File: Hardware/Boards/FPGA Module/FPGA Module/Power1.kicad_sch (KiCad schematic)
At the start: 84 parts, among them U10 TPS62933O, U12 INA700AYWFR, U13 INA700AYWFR, U14 INA700AYWFR, U15 INA700AYWFR, U16 INA700AYWFR, U18 INA236, U19 TPS74801AWDRC, U2 TPS62933O, U3 AOZ2369QI-11, U4 TPSM33625RDNR, U7 TPS62933O, U8 TPS62933O, U9 TPS62933O

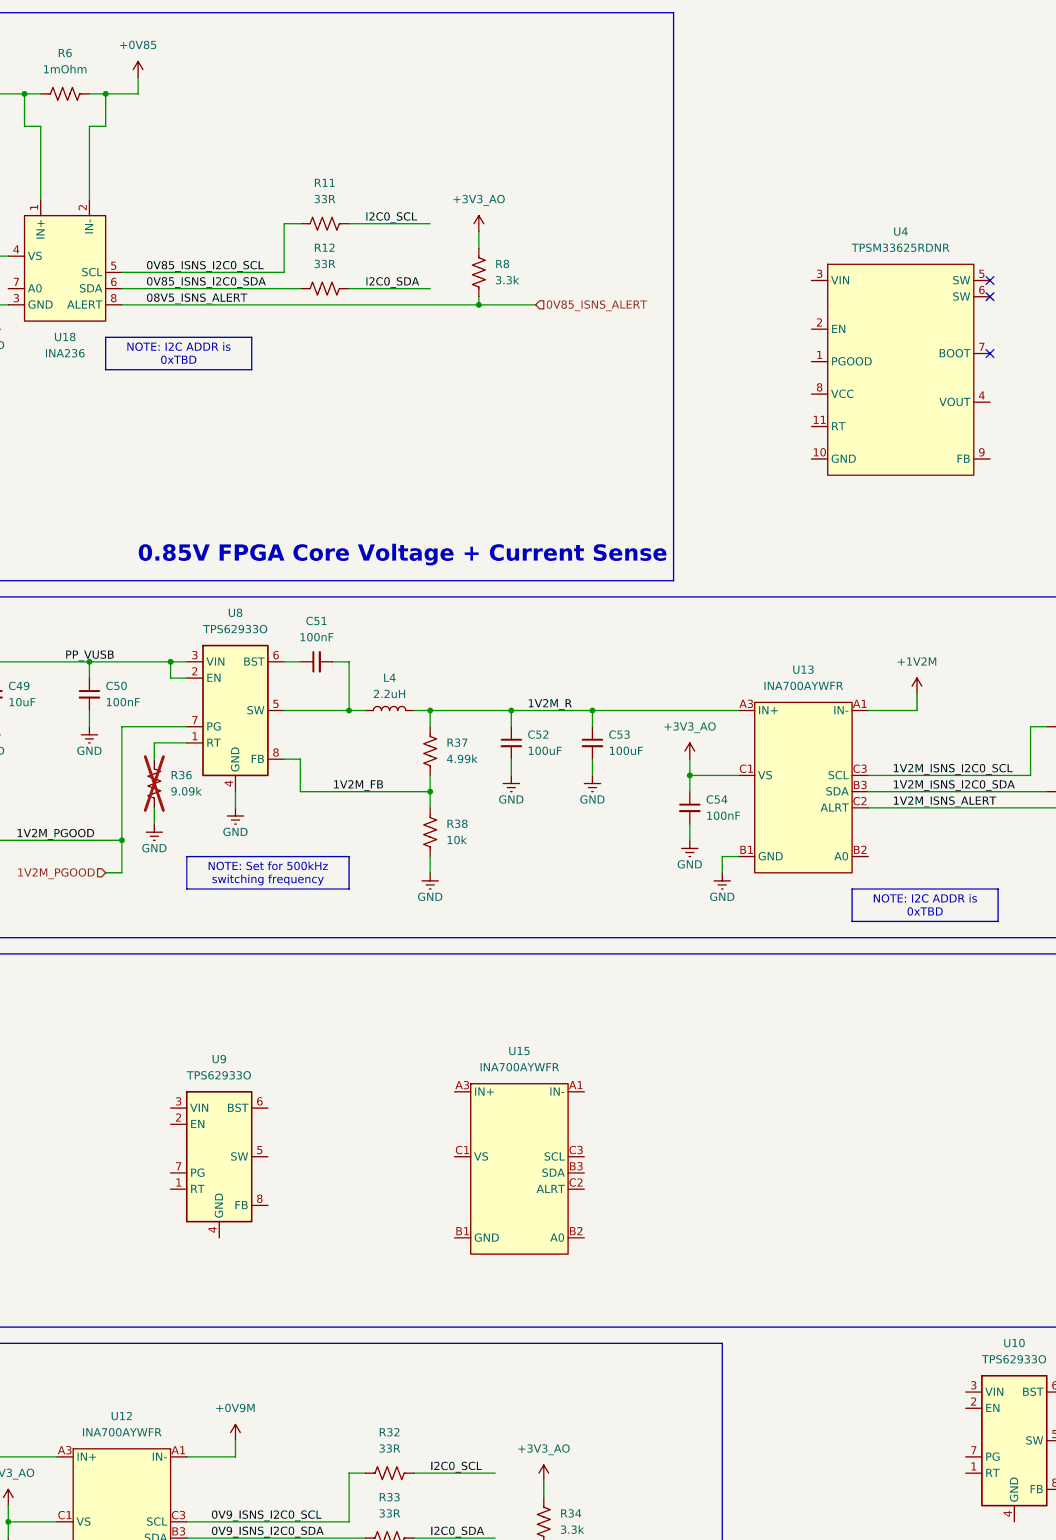
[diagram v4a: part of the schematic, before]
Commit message: Using new DP to HDMI IC
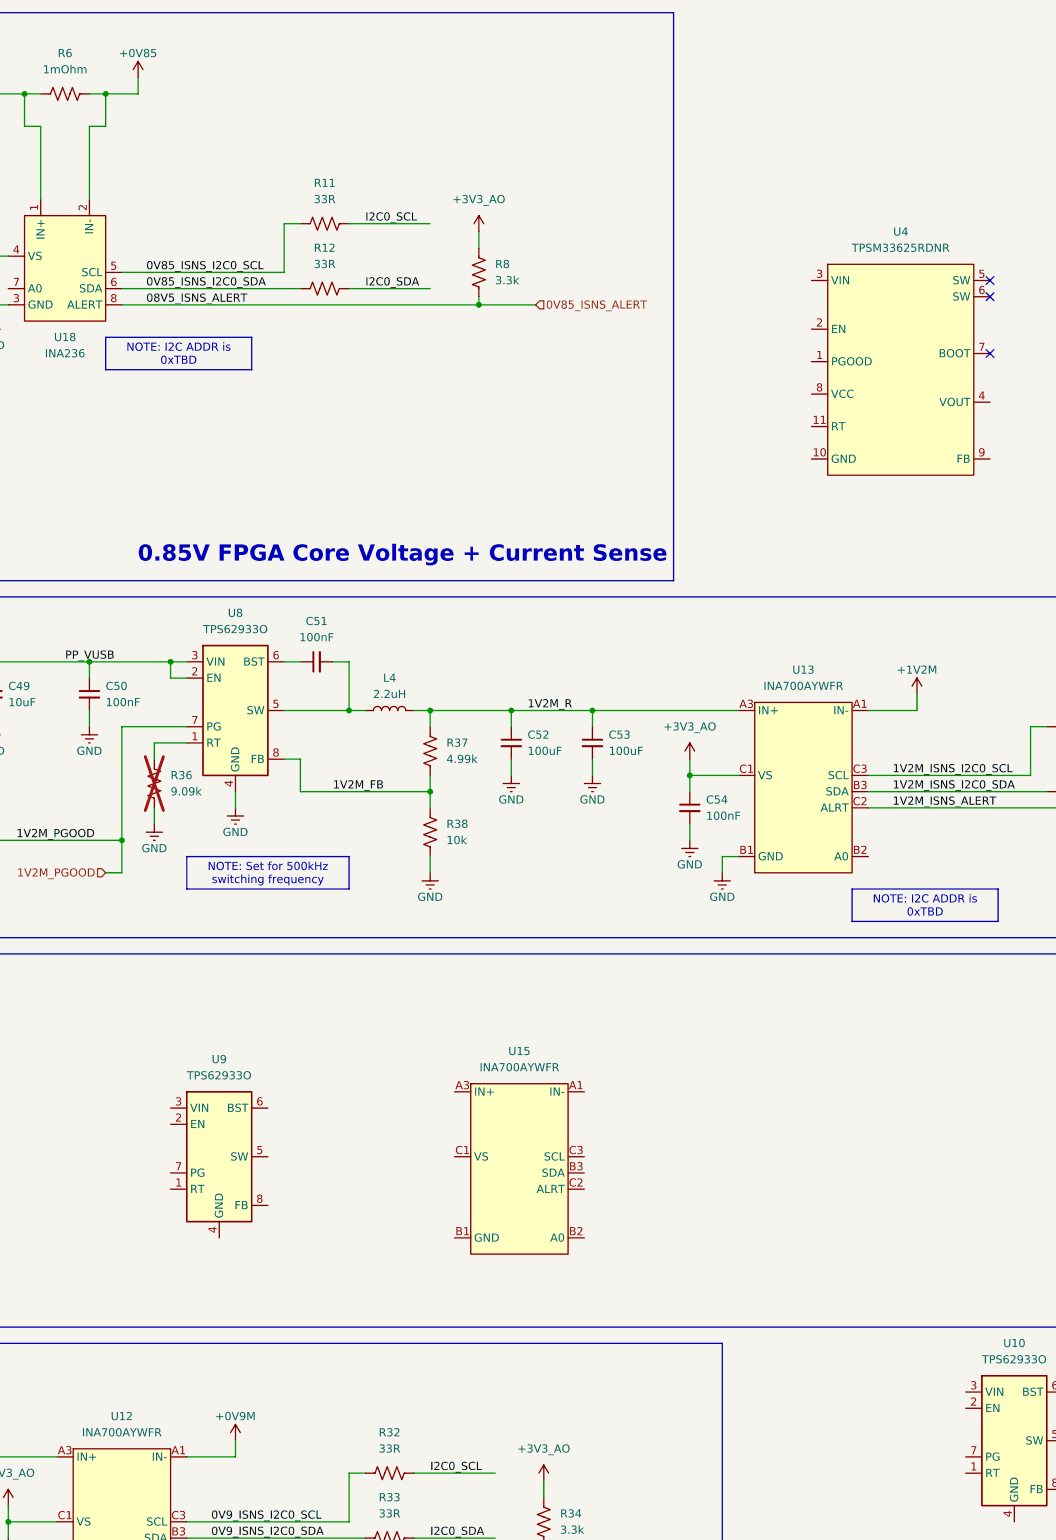
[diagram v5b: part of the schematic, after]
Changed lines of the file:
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@@
 		(on_board yes)
 		(dnp no)
-		(fields_autoplaced yes)
 		(property "Reference" "#PWR0100"
 			(at 297.18 125.73 0)
@@
 		)
 		(property "Value" "+1V2M"
-			(at 297.18 116.84 0)
+			(at 297.18 118.11 0)
 			(effects
 				(font
@@
 		(on_board yes)
 		(dnp no)
-		(fields_autoplaced yes)
 		(property "Reference" "#PWR085"
 			(at 190.5 242.57 0)
@@
 		)
 		(property "Value" "+0V9M"
-			(at 190.5 233.68 0)
+			(at 190.5 234.95 0)
 			(effects
 				(font
@@
 		(on_board yes)
 		(dnp no)
-		(fields_autoplaced yes)
 		(property "Reference" "#PWR027"
 			(at 175.26 29.21 0)
@@
 		)
 		(property "Value" "+0V85"
-			(at 175.26 20.32 0)
+			(at 175.26 21.59 0)
 			(effects
 				(font

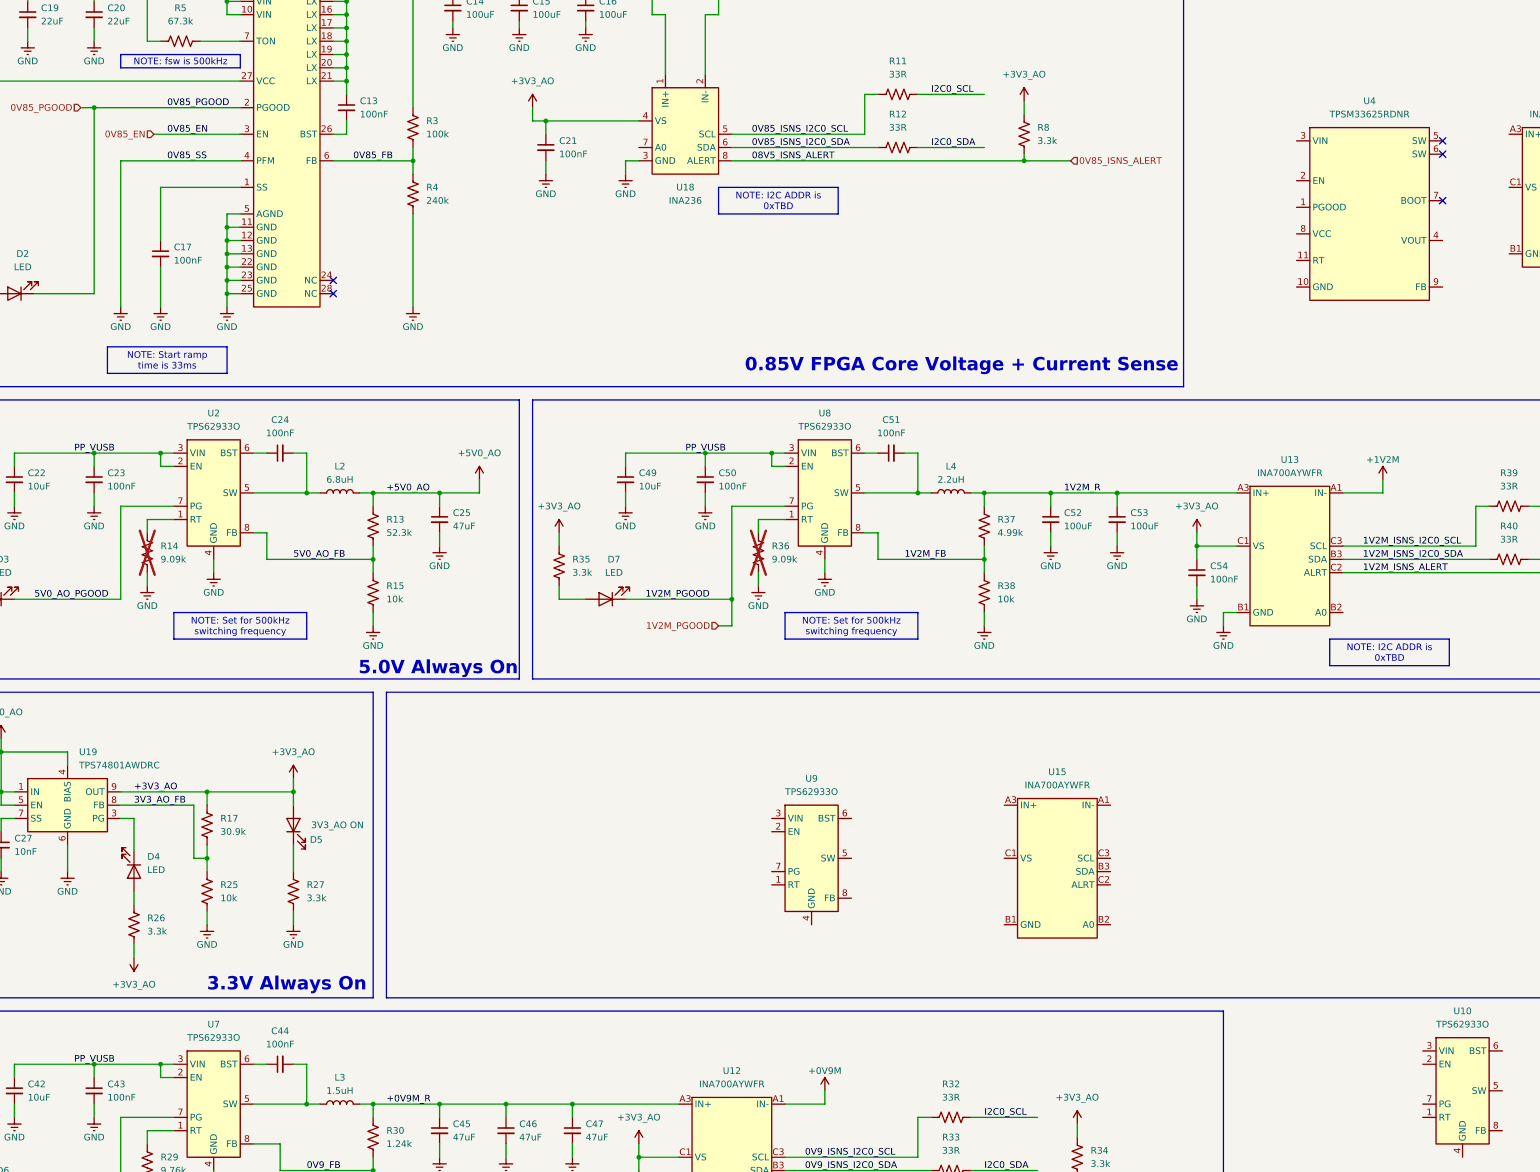
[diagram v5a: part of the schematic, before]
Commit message: minor FPGA schematic changes
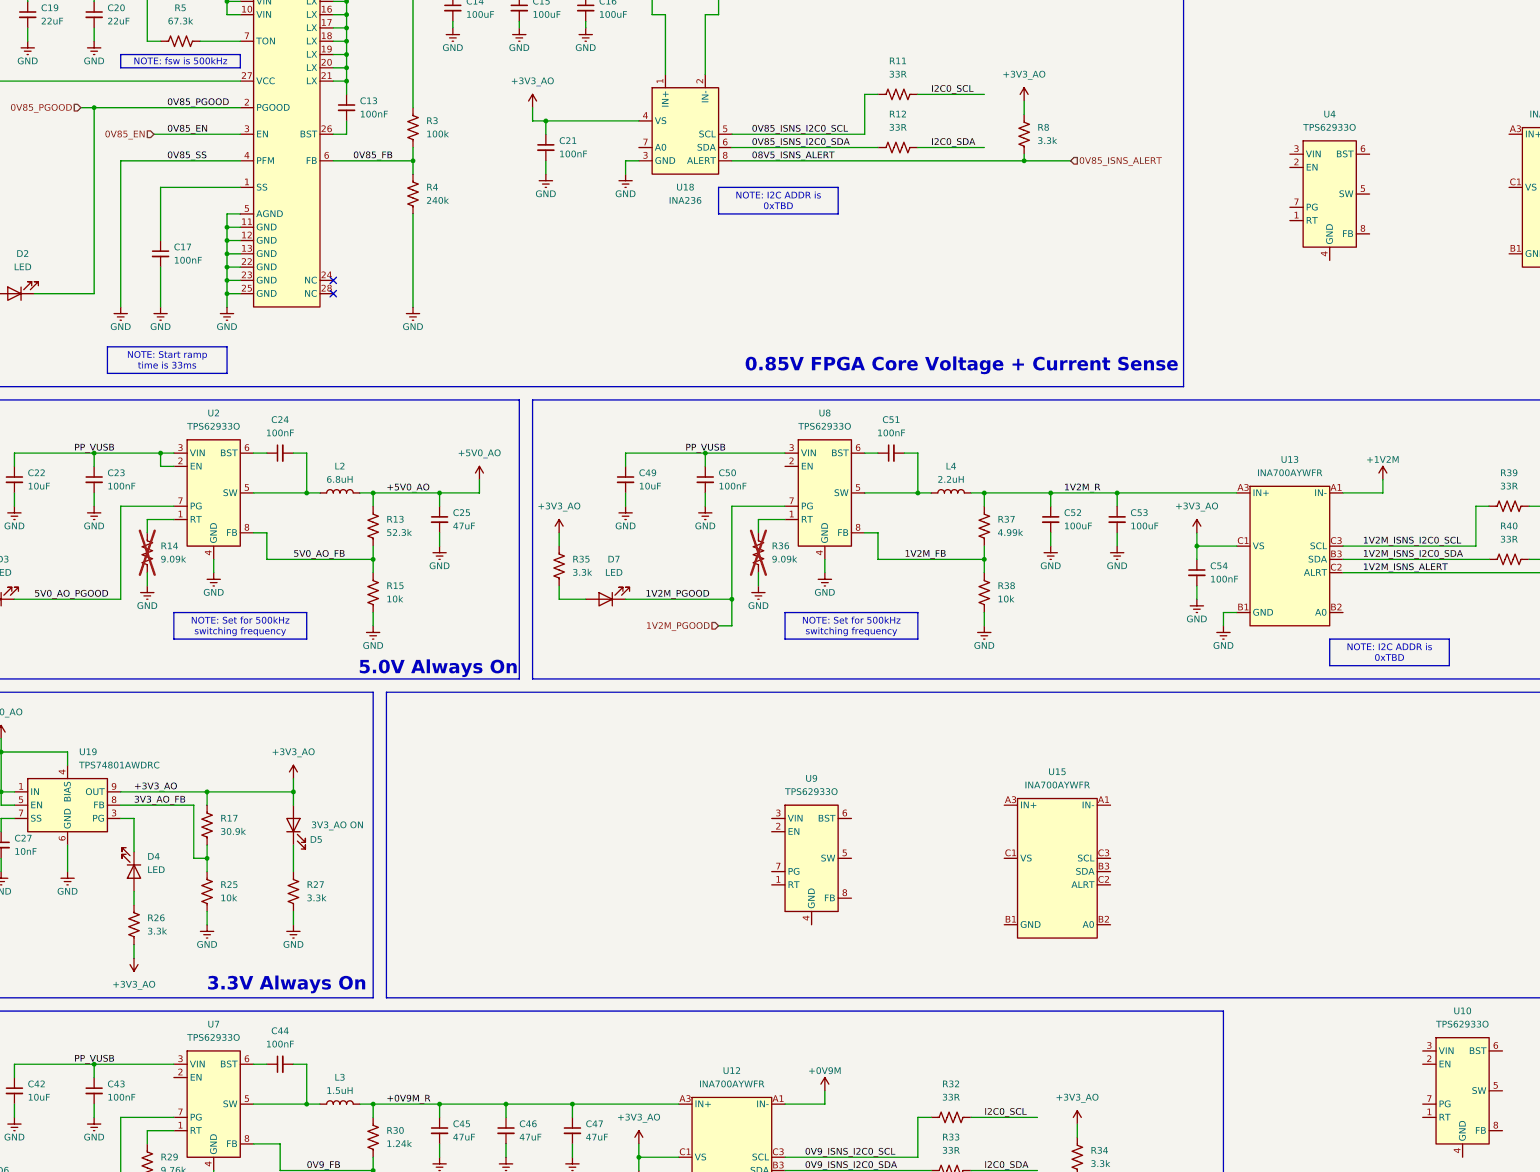
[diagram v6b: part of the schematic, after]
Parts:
- removed U4: TPSM33625RDNR, FPGA Module:RDN0011A-MFG, symbol FPGA Module:TPSM33625
- added U4: TPS62933O, Package_TO_SOT_SMD:SOT-583-8, symbol Regulator_Switching:TPS62933O
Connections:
- net PP_VUSB: no longer U7.2 (EN), U8.2 (EN)
- no-connect marks 5 -> 2
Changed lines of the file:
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@@
 	)
 	(junction
-		(at 63.5 233.68)
-		(diameter 0)
-		(color 0 0 0 0)
-	)
-	(junction
 		(at 76.2 30.48)
 		(diameter 0)
@@
 	)
 	(junction
-		(at 180.34 116.84)
-		(diameter 0)
-		(color 0 0 0 0)
-	)
-	(junction
 		(at 104.14 137.16)
 		(diameter 0)
@@
 		(at 96.52 86.36)
 	)
-	(no_connect
-		(at 308.61 59.69)
-	)
-	(no_connect
-		(at 308.61 68.58)
-	)
-	(no_connect
-		(at 308.61 57.15)
-	)
 	(wire
 		(pts
@@
 	(wire
 		(pts
-			(xy 66.04 233.68) (xy 63.5 233.68)
+			(xy 50.8 233.68) (xy 66.04 233.68)
 		)
 		(stroke
@@
 	(wire
 		(pts
-			(xy 63.5 233.68) (xy 50.8 233.68)
-		)
-		(stroke
-			(width 0)
-			(type default)
-		)
-	)
-	(wire
-		(pts
 			(xy 144.78 34.29) (xy 144.78 35.56)
 		)
@@
 	(wire
 		(pts
-			(xy 182.88 119.38) (xy 180.34 119.38)
-		)
-		(stroke
-			(width 0)
-			(type default)
-		)
-	)
-	(wire
-		(pts
 			(xy 233.68 124.46) (xy 246.38 124.46)
 		)
@@
 	(wire
 		(pts
-			(xy 182.88 116.84) (xy 180.34 116.84)
-		)
-		(stroke
-			(width 0)
-			(type default)
-		)
-	)
-	(wire
-		(pts
 			(xy 81.28 116.84) (xy 83.82 116.84)
 		)
@@
 	(wire
 		(pts
-			(xy 63.5 236.22) (xy 63.5 233.68)
-		)
-		(stroke
-			(width 0)
-			(type default)
-		)
-	)
-	(wire
-		(pts
 			(xy 22.86 181.61) (xy 22.86 184.15)
 		)
@@
 	(wire
 		(pts
-			(xy 66.04 236.22) (xy 63.5 236.22)
-		)
-		(stroke
-			(width 0)
-			(type default)
-		)
-	)
-	(wire
-		(pts
 			(xy 25.4 45.72) (xy 78.74 45.72)
 		)
@@
 	(wire
 		(pts
-			(xy 180.34 119.38) (xy 180.34 116.84)
-		)
-		(stroke
-			(width 0)
-			(type default)
-		)
-	)
-	(wire
-		(pts
 			(xy 177.8 129.54) (xy 177.8 132.08)
 		)
@@
 	(wire
 		(pts
-			(xy 180.34 116.84) (xy 167.64 116.84)
+			(xy 167.64 116.84) (xy 182.88 116.84)
 		)
 		(stroke
@@
 	)
 	(symbol
-		(lib_id "FPGA Module:TPSM33625")
-		(at 283.21 57.15 0)
-		(unit 1)
-		(exclude_from_sim no)
-		(in_bom yes)
-		(on_board yes)
-		(dnp no)
-		(fields_autoplaced yes)
-		(property "Reference" "U4"
-			(at 294.64 49.53 0)
-			(effects
-				(font
-					(size 1.27 1.27)
-				)
-			)
-		)
-		(property "Value" "TPSM33625RDNR"
-			(at 294.64 52.07 0)
-			(effects
-				(font
-					(size 1.27 1.27)
-				)
-			)
-		)
-		(property "Footprint" "FPGA Module:RDN0011A-MFG"
-			(at 294.64 91.44 0)
-			(effects
-				(font
-					(size 1.27 1.27)
-				)
-				(hide yes)
-			)
-		)
-		(property "Datasheet" "https://www.ti.com/lit/ds/symlink/tpsm33625.pdf"
-			(at 293.37 88.9 0)
-			(effects
-				(font
-					(size 1.27 1.27)
-				)
-				(hide yes)
-			)
-		)
-		(property "Description" ""
-			(at 283.21 57.15 0)
-			(effects
-				(font
-					(size 1.27 1.27)
-				)
-				(hide yes)
-			)
-		)
-		(pin "8"
-		)
-		(pin "1"
-		)
-		(pin "10"
-		)
-		(pin "3"
-		)
-		(pin "7"
-		)
-		(pin "6"
-		)
-		(pin "5"
-		)
-		(pin "4"
-		)
-		(pin "9"
-		)
-		(pin "2"
-		)
-		(pin "11"
-		)
-		(instances
-			(project ""
-				(path "/199f10e2-d4b4-4a27-9e84-7b1ce2ae6bf0/0c296310-f788-47f0-8a3f-43c3444563e8/e751a632-5f45-4f29-8d0a-1f9649251d32"
-					(reference "U4")
-					(unit 1)
-				)
-			)
-		)
-	)
-	(symbol
 		(lib_id "Device:R_US")
 		(at 72.39 187.96 0)
@@
 					(unit 1)
 				)
+			)
+		)
+	)
+	(symbol
+		(lib_id "Regulator_Switching:TPS62933O")
+		(at 287.02 67.31 0)
+		(unit 1)
+		(exclude_from_sim no)
+		(in_bom yes)
+		(on_board yes)
+		(dnp no)
+		(fields_autoplaced yes)
+		(property "Reference" "U4"
+			(at 287.02 52.07 0)
+			(effects
+				(font
+					(size 1.27 1.27)
+				)
+			)
+		)
+		(property "Value" "TPS62933O"
+			(at 287.02 54.61 0)
+			(effects
+				(font
+					(size 1.27 1.27)
+				)
+			)
+		)
+		(property "Footprint" "Package_TO_SOT_SMD:SOT-583-8"
+			(at 287.02 92.71 0)
+			(effects
+				(font
+					(size 1.27 1.27)
+				)
+				(hide yes)
+			)
+		)
+		(property "Datasheet" "https://www.ti.com/lit/ds/symlink/tps62933.pdf"
+			(at 287.02 90.17 0)
+			(effects
+				(font
+					(size 1.27 1.27)
+				)
+				(hide yes)
+			)
+		)
+		(property "Description" "3.8-30V, 3A Synchronous Buck Converters with out of audio (OOA) mode and power good, SOT583-8"
+			(at 287.02 67.31 0)
+			(effects
+				(font
+					(size 1.27 1.27)
+				)
+				(hide yes)
+			)
+		)
+		(pin "7"
+		)
+		(pin "8"
+		)
+		(pin "3"
+		)
+		(pin "6"
+		)
+		(pin "5"
+		)
+		(pin "2"
+		)
+		(pin "1"
+		)
+		(pin "4"
+		)
+		(instances
+			(project "FPGA Module"
+				(path "/199f10e2-d4b4-4a27-9e84-7b1ce2ae6bf0/0c296310-f788-47f0-8a3f-43c3444563e8/e751a632-5f45-4f29-8d0a-1f9649251d32"
+					(reference "U4")
+					(unit 1)
+				)

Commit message: updated fpga module schematics
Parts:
- removed C13, C17, C21, C23, C24, C43, C44, C48, C50, C51, C54: 100nF, Capacitor_SMD:C_0402_1005Metric, symbol Device:C_Small
- removed C14, C15, C16, C52, C53: 100uF, Capacitor_SMD:C_0805_2012Metric, symbol Device:C_Small
- removed C18: 4.7uF, Capacitor_SMD:C_0402_1005Metric, symbol Device:C_Small
- removed C19, C20: 22uF, Capacitor_SMD:C_0805_2012Metric, symbol Device:C_Small
- removed C22, C42, C49: 10uF, Capacitor_SMD:C_0603_1608Metric, symbol Device:C_Small
- removed C25, C45, C46, C47: 47uF, Capacitor_SMD:C_0603_1608Metric, symbol Device:C_Small
- removed D2, D3, D6, D7: LED, LED_SMD:LED_0603_1608Metric, symbol Device:LED
- removed L1: 0.47uH, FPGA Module:INDM135125X500N, symbol Device:L
- removed L2: 6.8uH, FPGA Module:THMC0503SP-6R8MG-D, symbol Device:L
- removed L3: 1.5uH, FPGA Module:SRU1038100Y, symbol Device:L
- removed L4: 2.2uH, FPGA Module:SRU10382R2Y, symbol Device:L
- removed R10, R16, R28, R34, R35, R41, R7, R8, R9: 3.3k, Resistor_SMD:R_0402_1005Metric, symbol Device:R_US
- removed R11, R12, R32, R33, R39, R40: 33R, Resistor_SMD:R_0402_1005Metric, symbol Device:R_US
- removed R13: 52.3k, Resistor_SMD:R_0402_1005Metric, symbol Device:R_US
- removed R14, R36: 9.09k, Resistor_SMD:R_0402_1005Metric, symbol Device:R_US
- removed R15, R31, R38: 10k, Resistor_SMD:R_0402_1005Metric, symbol Device:R_US
- removed R29: 9.76k, Resistor_SMD:R_0402_1005Metric, symbol Device:R_US
- removed R3: 100k, Resistor_SMD:R_0402_1005Metric, symbol Device:R_US
- removed R30: 1.24k, Resistor_SMD:R_0402_1005Metric, symbol Device:R_US
- removed R37: 4.99k, Resistor_SMD:R_0402_1005Metric, symbol Device:R_US
- removed R4: 240k, Resistor_SMD:R_0402_1005Metric, symbol Device:R_US
- removed R5: 67.3k, Resistor_SMD:R_0402_1005Metric, symbol Device:R_US
- removed R6: 1mOhm, Resistor_SMD:R_1206_3216Metric, symbol Device:R_US
- removed U10, U2, U4, U7, U8, U9: TPS62933O, Package_TO_SOT_SMD:SOT-583-8, symbol Regulator_Switching:TPS62933O
- removed U12, U13, U14, U15, U16: INA700AYWFR, FPGA Module:INA700_AYWFR, symbol FPGA Module:INA700
- removed U18: INA236, Package_TO_SOT_SMD:SOT-23-8, symbol FPGA Module:INA236
- removed U3: AOZ2369QI-11, FPGA Module:AOZ2369QI11, symbol FPGA Module:AOZ2369QI-11
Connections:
- no-connect marks 2 -> 0
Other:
- note removed: "0.9V MGTAVCC"
- note removed: "5.0V Always On"
